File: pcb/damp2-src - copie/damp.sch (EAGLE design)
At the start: 24 parts, among them IC2 74C74N, K1 G5L, Q3 BSS138, Q5 BSS138

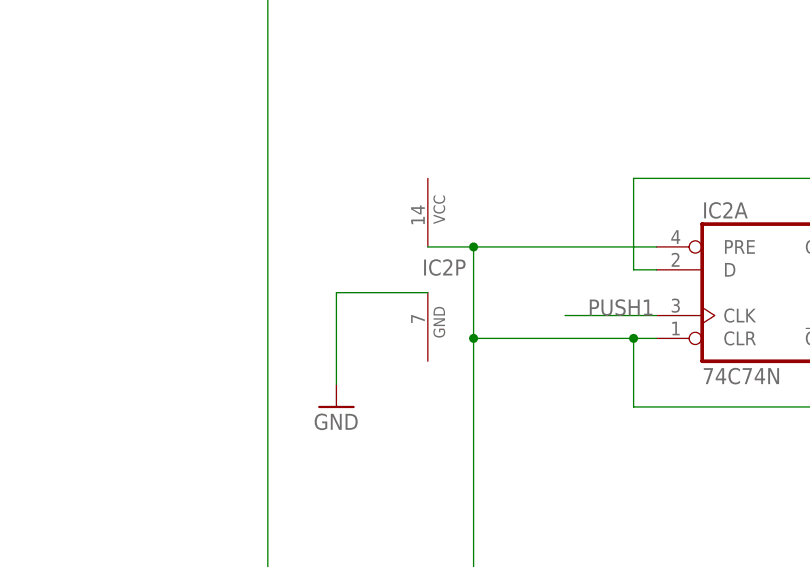
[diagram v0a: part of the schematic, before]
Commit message: minor debug (hole + value)
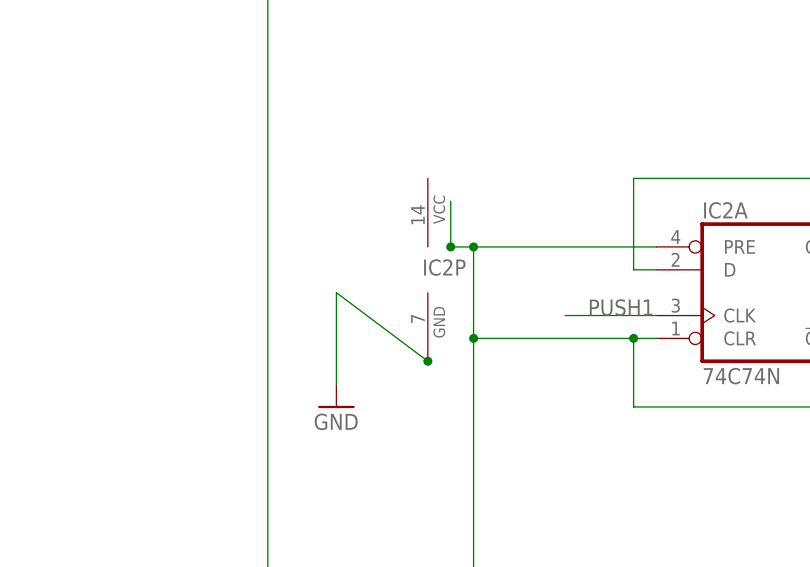
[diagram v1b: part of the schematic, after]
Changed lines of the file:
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@@
 </segment>
 <segment>
-<wire x1="177.8" y1="43.18" x2="167.64" y2="43.18" width="0.1524" layer="91"/>
+<wire x1="177.8" y1="35.56" x2="167.64" y2="43.18" width="0.1524" layer="91"/>
 <wire x1="167.64" y1="43.18" x2="167.64" y2="33.02" width="0.1524" layer="91"/>
 <pinref part="GND12" gate="1" pin="GND"/>
+<junction x="177.8" y="35.56"/>
 </segment>
 <segment>
@@
 <wire x1="200.66" y1="2.54" x2="200.66" y2="7.62" width="0.1524" layer="91"/>
 <junction x="195.58" y="7.62"/>
-<wire x1="177.8" y1="48.26" x2="182.88" y2="48.26" width="0.1524" layer="91"/>
+<wire x1="180.34" y1="48.26" x2="182.88" y2="48.26" width="0.1524" layer="91"/>
 <wire x1="182.88" y1="48.26" x2="182.88" y2="38.1" width="0.1524" layer="91"/>
 <junction x="182.88" y="7.62"/>
@@
 <wire x1="160.02" y1="119.38" x2="111.76" y2="119.38" width="0.1524" layer="91"/>
 <wire x1="111.76" y1="119.38" x2="111.76" y2="109.22" width="0.1524" layer="91"/>
+<junction x="180.34" y="48.26"/>
+<wire x1="180.34" y1="53.34" x2="180.34" y2="48.26" width="0.1524" layer="91"/>
 </segment>
 </net>
